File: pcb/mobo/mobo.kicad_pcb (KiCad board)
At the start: 2 copper layers, 51.6 x 89 mm, 73 parts, among them J1 ISP, J2 PEEL_MOTOR, J3 DRIVE_MOTOR, J4 SW1, J5 SPRING_FINGERS, J6 SW2, J8 USART1, U1 ATmega328PB-A, U2 ATmega328PB-M, U4 AP1117-50, U5 MC34063AD, U6 SP308xE, U7 DRV8837, U8 DRV8837, Y1 16MHz

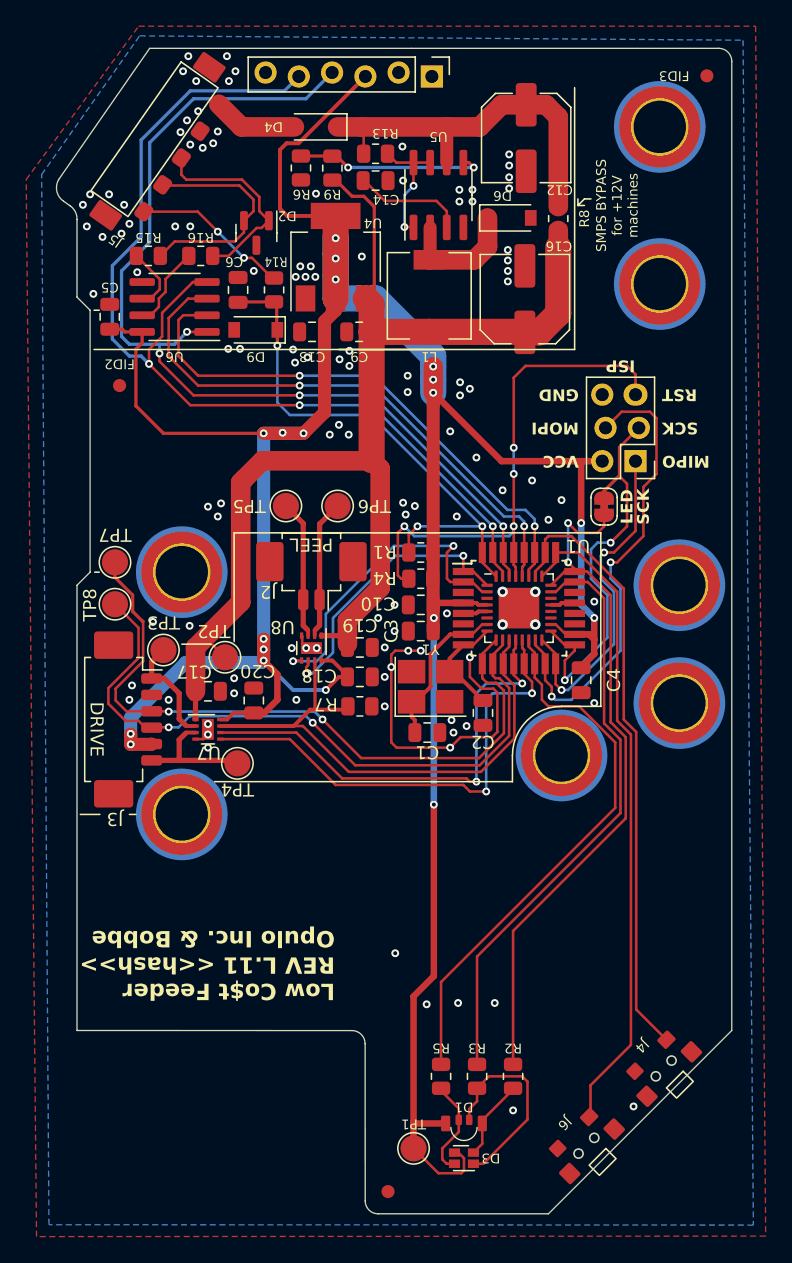
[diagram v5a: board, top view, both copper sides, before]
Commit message: Remove vias from pads, Remove paste layer from alt QFN footprint (#14)
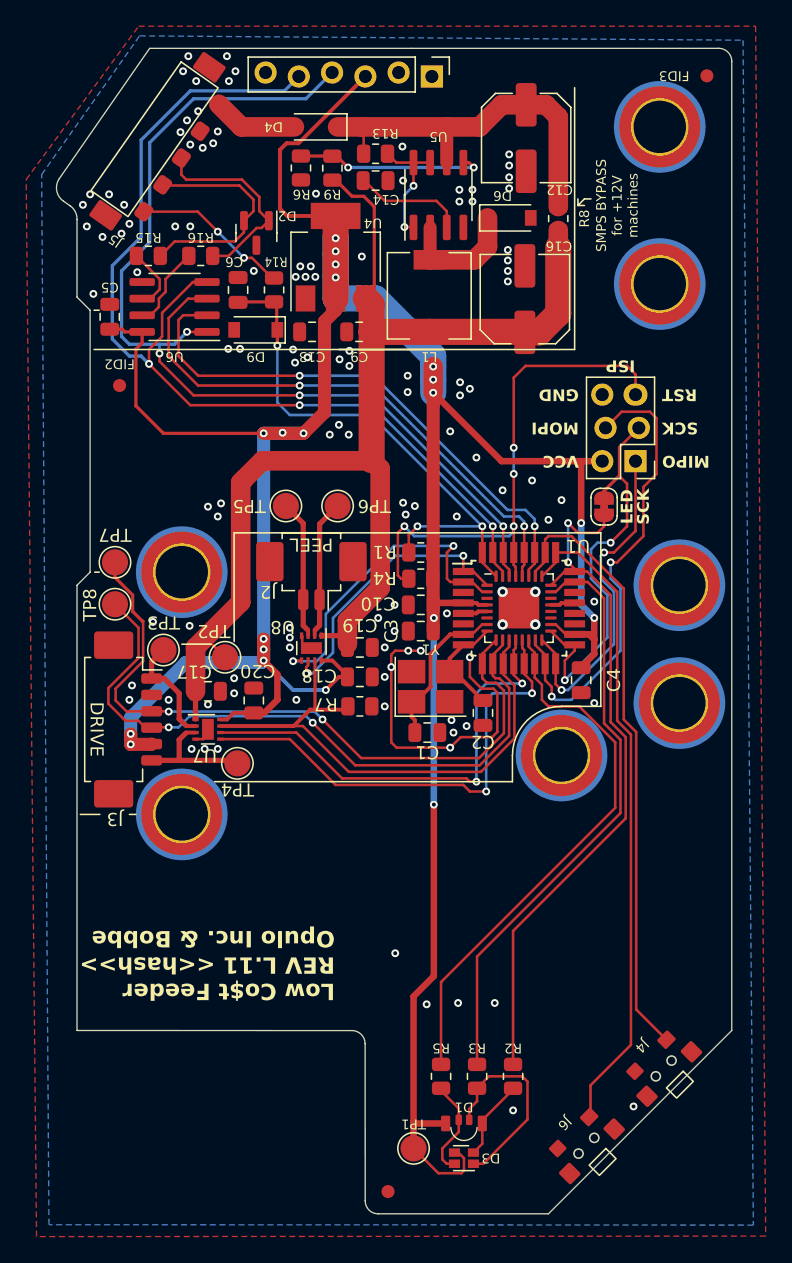
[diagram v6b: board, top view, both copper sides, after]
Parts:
- U2: footprint Package_DFN_QFN:QFN-32-1EP_5x5mm_P0.5mm_EP3.1x3.1mm -> feeder:QFN-32-1EP_5x5mm_P0.5mm_EP3.1x3.1mm_DNP
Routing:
- net GND: vias 117 -> 118
- net +5V: vias 19 -> 20

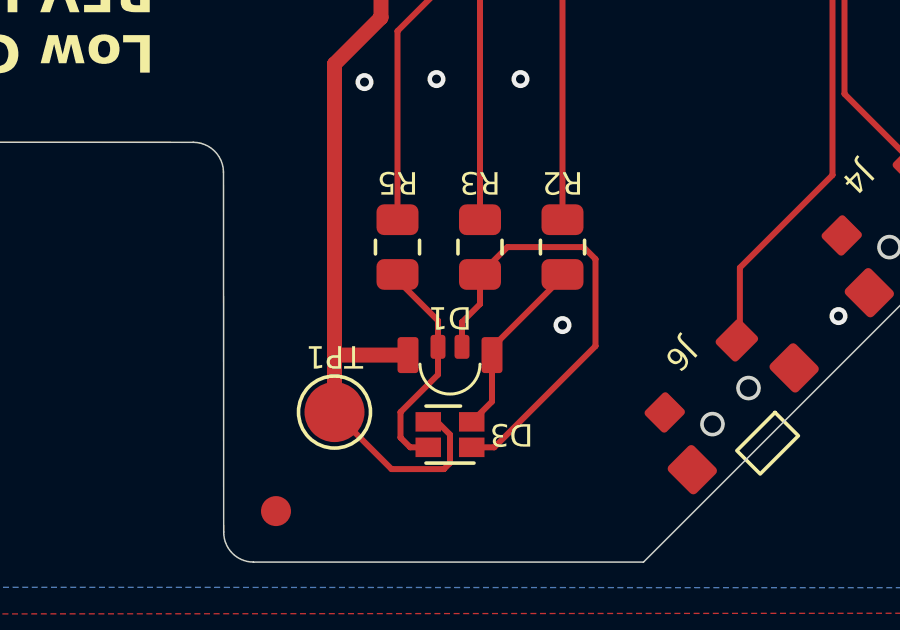
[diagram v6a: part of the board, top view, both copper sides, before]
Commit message: Mark LED_RGBA_ALT as DNP, Add MHS110FRGBCT symbol, footprint (#9)
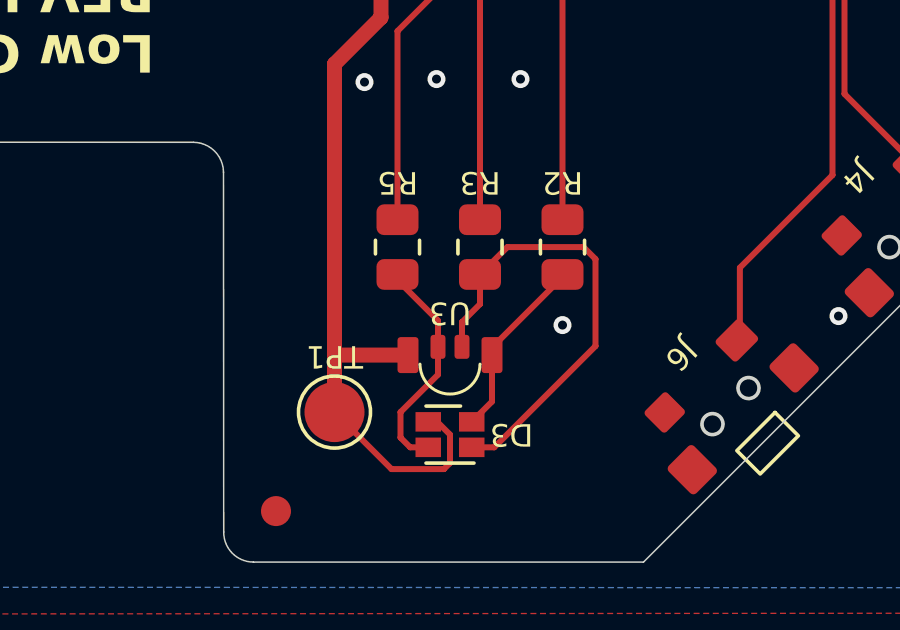
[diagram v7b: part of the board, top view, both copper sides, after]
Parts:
- U3: renamed from D1; value LED_RGBA -> LED_RGB; footprint index:MHS110FRGBCT -> feeder:MHS110FRGBCT
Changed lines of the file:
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@@
   (net 19 "DRIVE1")
   (net 20 "DE")
-  (net 21 "Net-(D1-GK)")
-  (net 22 "Net-(D1-BK)")
-  (net 23 "Net-(D1-A)")
+  (net 21 "Net-(D3-RK)")
+  (net 22 "Net-(D3-GK)")
+  (net 23 "Net-(D3-BK)")
   (net 24 "Net-(D6-K)")
   (net 25 "Net-(J5-Pin_5)")
@@
     )
   )
-  (footprint "index:MHS110FRGBCT" (layer "F.Cu")
+  (footprint "feeder:MHS110FRGBCT" (layer "F.Cu")
     (at 130.85 112.3)
     (property "Sheetfile" "mobo.kicad_sch")
     (property "Sheetname" "")
-    (property "ki_description" "RGB LED, red/green/blue/anode")
-    (property "ki_keywords" "LED RGB diode")
     (attr smd)
-    (fp_text reference "D1" (at 0 -1.65 180 unlocked) (layer "F.SilkS")
+    (fp_text reference "U3" (at 0 -1.8 180 unlocked) (layer "F.SilkS")
         (effects (font (size 0.75 0.75) (thickness 0.1)))
     )
-    (fp_text value "LED_RGBA" (at 0 1 unlocked) (layer "F.Fab")
+    (fp_text value "LED_RGB" (at 0 1 unlocked) (layer "F.Fab")
         (effects (font (size 1 1) (thickness 0.15)))
     )
@@
       (stroke (width 0.1) (type solid)) (layer "F.SilkS"))
     (pad "1" smd roundrect (at -1.4 -0.4) (size 0.7 1.2) (layers "F.Cu" "F.Paste" "F.Mask") (roundrect_rratio 0.1428571429)
-      (net 11 "+5V") (pinfunction "RK") (pintype "passive"))
+      (net 11 "+5V") (pinfunction "VCC") (pintype "unspecified"))
     (pad "2" smd roundrect (at -0.4 -0.675) (size 0.5 0.8) (layers "F.Cu" "F.Paste" "F.Mask") (roundrect_rratio 0.2)
-      (net 21 "Net-(D1-GK)") (pinfunction "GK") (pintype "passive"))
+      (net 23 "Net-(D3-BK)") (pinfunction "B") (pintype "unspecified"))
     (pad "3" smd roundrect (at 0.4 -0.675) (size 0.5 0.8) (layers "F.Cu" "F.Paste" "F.Mask") (roundrect_rratio 0.2)
-      (net 22 "Net-(D1-BK)") (pinfunction "BK") (pintype "passive"))
+      (net 22 "Net-(D3-GK)") (pinfunction "G") (pintype "unspecified"))
     (pad "4" smd roundrect (at 1.4 -0.4) (size 0.7 1.2) (layers "F.Cu" "F.Paste" "F.Mask") (roundrect_rratio 0.1428571429)
-      (net 23 "Net-(D1-A)") (pinfunction "A") (pintype "passive"))
+      (net 21 "Net-(D3-RK)") (pinfunction "R") (pintype "unspecified"))
   )
   (footprint "Package_SON:WSON-8-1EP_2x2mm_P0.5mm_EP0.9x1.6mm" (layer "F.Cu")
@@
       (net 38 "LED_B") (pintype "passive"))
     (pad "2" smd roundrect (at 0.9125 0 270) (size 1.025 1.4) (layers "F.Cu" "F.Paste" "F.Mask") (roundrect_rratio 0.243902439)
-      (net 21 "Net-(D1-GK)") (pintype "passive"))
+      (net 23 "Net-(D3-BK)") (pintype "passive"))
     (model "${KICAD6_3DMODEL_DIR}/Resistor_SMD.3dshapes/R_0805_2012Metric.wrl"
       (offset (xyz 0 0 0))
@@
       (net 37 "LED_G") (pintype "passive"))
     (pad "2" smd roundrect (at 0.9125 0 270) (size 1.025 1.4) (layers "F.Cu" "F.Paste" "F.Mask") (roundrect_rratio 0.243902439)
-      (net 22 "Net-(D1-BK)") (pintype "passive"))
+      (net 22 "Net-(D3-GK)") (pintype "passive"))
     (model "${KICAD6_3DMODEL_DIR}/Resistor_SMD.3dshapes/R_0805_2012Metric.wrl"
       (offset (xyz 0 0 0))
@@
       (net 41 "LED_R") (pintype "passive"))
     (pad "2" smd roundrect (at 0.9125 0 270) (size 1.025 1.4) (layers "F.Cu" "F.Paste" "F.Mask") (roundrect_rratio 0.243902439)
-      (net 23 "Net-(D1-A)") (pintype "passive"))
+      (net 21 "Net-(D3-RK)") (pintype "passive"))
     (model "${KICAD6_3DMODEL_DIR}/Resistor_SMD.3dshapes/R_0805_2012Metric.wrl"
       (offset (xyz 0 0 0))
@@
     (property "Sheetfile" "mobo.kicad_sch")
     (property "Sheetname" "")
+    (property "dnp" "")
     (property "ki_description" "RGB LED, red/green/blue/anode")
     (property "ki_keywords" "LED RGB diode")
@@
       (stroke (width 0.1) (type solid)) (layer "F.Fab"))
     (pad "1" smd rect (at -0.425 -0.725 270) (size 0.65 0.85) (layers "F.Cu" "F.Paste" "F.Mask")
-      (net 23 "Net-(D1-A)") (pinfunction "RK") (pintype "passive"))
+      (net 21 "Net-(D3-RK)") (pinfunction "RK") (pintype "passive"))
     (pad "2" smd rect (at 0.425 -0.725 270) (size 0.65 0.85) (layers "F.Cu" "F.Paste" "F.Mask")
-      (net 22 "Net-(D1-BK)") (pinfunction "GK") (pintype "passive"))
+      (net 22 "Net-(D3-GK)") (pinfunction "GK") (pintype "passive"))
     (pad "3" smd rect (at 0.425 0.725 270) (size 0.65 0.85) (layers "F.Cu" "F.Paste" "F.Mask")
-      (net 21 "Net-(D1-GK)") (pinfunction "BK") (pintype "passive"))
+      (net 23 "Net-(D3-BK)") (pinfunction "BK") (pintype "passive"))
     (pad "4" smd rect (at -0.425 0.725 270) (size 0.65 0.85) (layers "F.Cu" "F.Paste" "F.Mask")
       (net 11 "+5V") (pinfunction "A") (pintype "passive"))
@@
   (segment (start 135.05 65.55) (end 135.45 65.95) (width 0.2) (layer "B.Cu") (net 20))
   (segment (start 118.3 55.55) (end 123.9 55.55) (width 0.2) (layer "B.Cu") (net 20))
-  (segment (start 130.45 111.625) (end 130.45 112.550978) (width 0.2) (layer "F.Cu") (net 21))
-  (segment (start 130.45 112.550978) (end 129.2 113.800978) (width 0.2) (layer "F.Cu") (net 21))
-  (segment (start 129.2 113.800978) (end 129.2 114.65) (width 0.2) (layer "F.Cu") (net 21))
-  (segment (start 129.2 114.65) (end 129.525 114.975) (width 0.2) (layer "F.Cu") (net 21))
-  (segment (start 130.45 110.75) (end 129.1 109.4) (width 0.2) (layer "F.Cu") (net 21))
-  (segment (start 130.45 111.625) (end 130.45 110.75) (width 0.2) (layer "F.Cu") (net 21))
-  (segment (start 129.525 114.975) (end 130.125 114.975) (width 0.2) (layer "F.Cu") (net 21))
+  (segment (start 131.575 114.125) (end 132.25 113.45) (width 0.2) (layer "F.Cu") (net 21))
+  (segment (start 134.6 109.3) (end 132.25 111.65) (width 0.2) (layer "F.Cu") (net 21))
+  (segment (start 132.25 113.45) (end 132.25 111.9) (width 0.2) (layer "F.Cu") (net 21))
   (segment (start 131.85 109.2125) (end 131.85 110.2) (width 0.2) (layer "F.Cu") (net 22))
   (segment (start 135.7 111.6) (end 135.7 108.7) (width 0.2) (layer "F.Cu") (net 22))
@@
   (segment (start 132.325 114.975) (end 135.7 111.6) (width 0.2) (layer "F.Cu") (net 22))
   (segment (start 135.3 108.3) (end 132.7625 108.3) (width 0.2) (layer "F.Cu") (net 22))
-  (segment (start 131.575 114.125) (end 132.25 113.45) (width 0.2) (layer "F.Cu") (net 23))
-  (segment (start 134.6 109.3) (end 132.25 111.65) (width 0.2) (layer "F.Cu") (net 23))
-  (segment (start 132.25 113.45) (end 132.25 111.9) (width 0.2) (layer "F.Cu") (net 23))
+  (segment (start 130.45 111.625) (end 130.45 112.550978) (width 0.2) (layer "F.Cu") (net 23))
+  (segment (start 130.45 112.550978) (end 129.2 113.800978) (width 0.2) (layer "F.Cu") (net 23))
+  (segment (start 129.2 113.800978) (end 129.2 114.65) (width 0.2) (layer "F.Cu") (net 23))
+  (segment (start 129.2 114.65) (end 129.525 114.975) (width 0.2) (layer "F.Cu") (net 23))
+  (segment (start 130.45 110.75) (end 129.1 109.4) (width 0.2) (layer "F.Cu") (net 23))
+  (segment (start 130.45 111.625) (end 130.45 110.75) (width 0.2) (layer "F.Cu") (net 23))
+  (segment (start 129.525 114.975) (end 130.125 114.975) (width 0.2) (layer "F.Cu") (net 23))
   (segment (start 132.65 44.95) (end 131.65 45.95) (width 1.5) (layer "F.Cu") (net 24))
   (segment (start 128.265 45.885) (end 128.2 45.95) (width 1.5) (layer "F.Cu") (net 24))

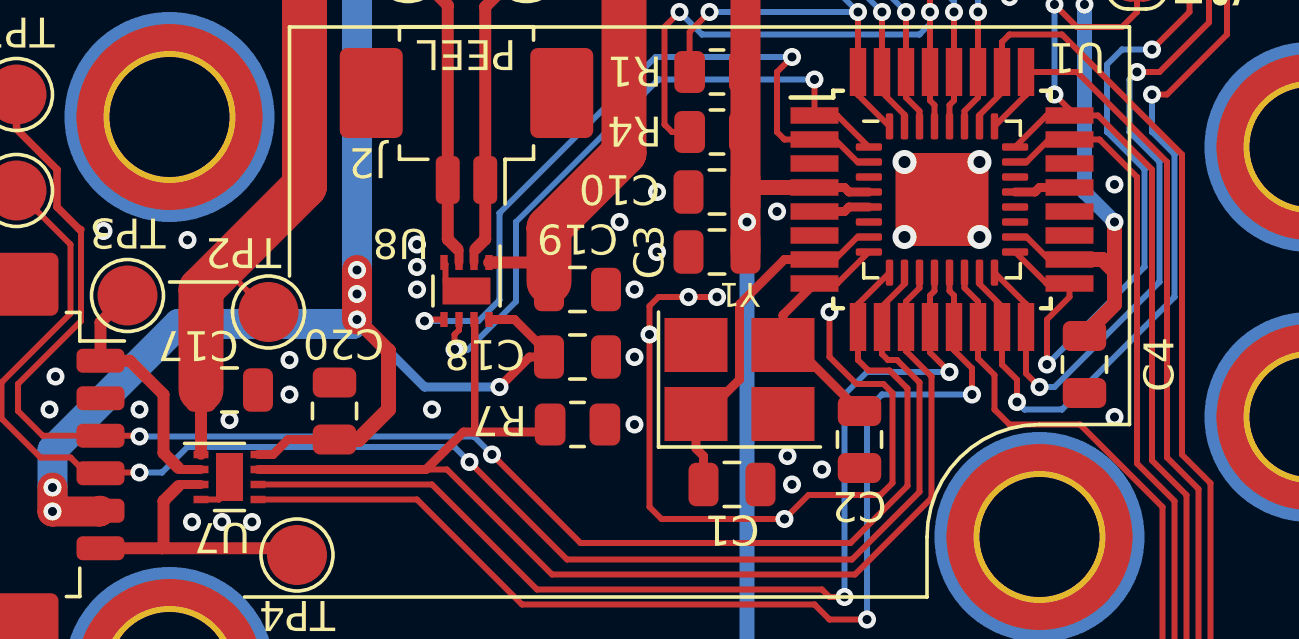
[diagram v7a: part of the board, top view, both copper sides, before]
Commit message: Improve driver power routing by adding filled zones
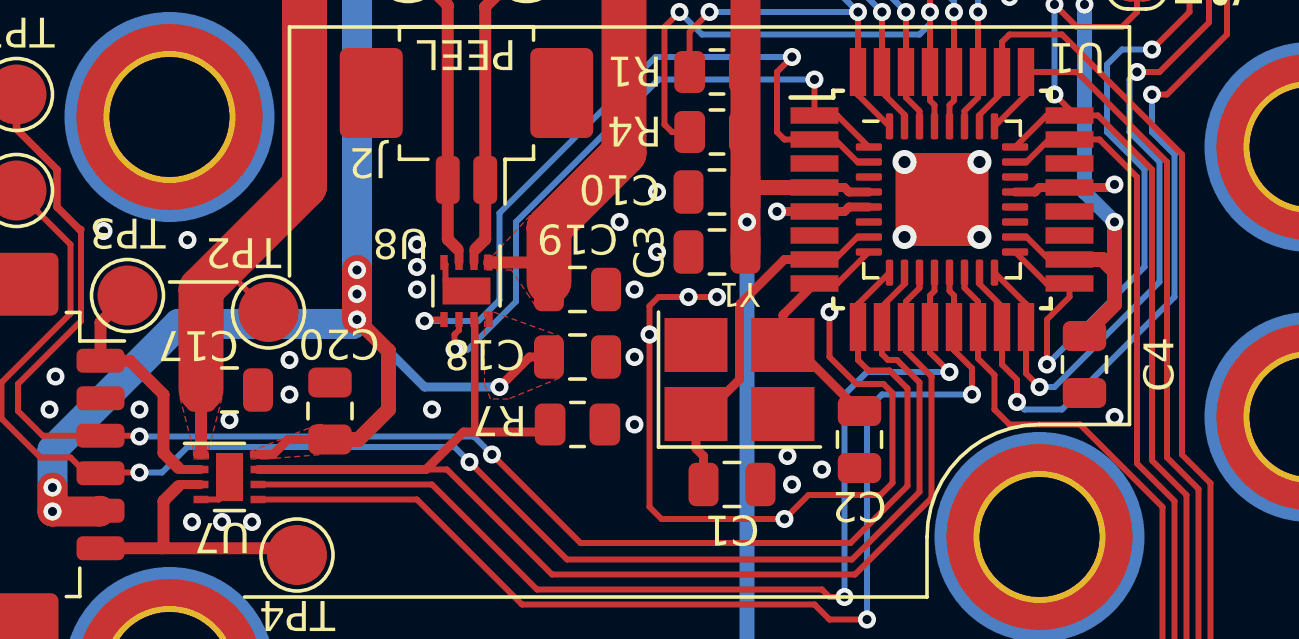
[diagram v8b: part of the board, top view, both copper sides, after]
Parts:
- moved C20 0.15 mm to (114.7, 79.6)
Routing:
- net GND: track 30.4 -> 33.2 mm
- net +5V: track 242.0 -> 239.5 mm
- added copper zone on F.Cu, net (none)
- added copper zone on F.Cu, net +10V
- added copper zone on F.Cu, net +5V
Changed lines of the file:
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@@
   )
   (footprint "Capacitor_SMD:C_0805_2012Metric" (layer "F.Cu")
-    (at 114.8 79.6 -90)
+    (at 114.65 79.6 -90)
     (descr "Capacitor SMD 0805 (2012 Metric), square (rectangular) end terminal, IPC_7351 nominal, (Body size source: IPC-SM-782 page 76, https://www.pcb-3d.com/wordpress/wp-content/uploads/ipc-sm-782a_amendment_1_and_2.pdf, https://docs.google.com/spreadsheets/d/1BsfQQcO9C6DZCsRaXUlFlo91Tg2WpOkGARC1WS5S8t0/edit?usp=sharing), generated with kicad-footprint-generator")
     (tags "capacitor")
@@
   )
   (segment (start 125.3 82.8) (end 125.3 76.1) (width 0.2) (layer "F.Cu") (net 1))
+  (segment (start 140.7 72.15) (end 140.8 72.05) (width 0.3) (layer "F.Cu") (net 1))
   (segment (start 129.8 83.2) (end 125.7 83.2) (width 0.2) (layer "F.Cu") (net 1))
   (segment (start 132.6125 72.8) (end 131.95 72.8) (width 0.3) (layer "F.Cu") (net 1))
@@
   (segment (start 131.95 72.8) (end 131.8 72.95) (width 0.3) (layer "F.Cu") (net 1))
   (segment (start 133.4 79) (end 133.4 82) (width 0.2) (layer "F.Cu") (net 1))
+  (segment (start 130.8 72.95) (end 129.55 72.95) (width 0.3) (layer "F.Cu") (net 1))
   (segment (start 133.4 82) (end 133 82.4) (width 0.2) (layer "F.Cu") (net 1))
   (segment (start 125.3 76.1) (end 125.6 75.8) (width 0.2) (layer "F.Cu") (net 1))
+  (segment (start 139.3 72.15) (end 140.7 72.15) (width 0.3) (layer "F.Cu") (net 1))
   (segment (start 138.3 72.15) (end 139.3 72.15) (width 0.3) (layer "F.Cu") (net 1))
   (segment (start 131.8 72.95) (end 130.8 72.95) (width 0.3) (layer "F.Cu") (net 1))
@@
   (segment (start 140.8 74.95) (end 140.4 74.55) (width 0.5) (layer "F.Cu") (net 11))
   (segment (start 130.85 114.55) (end 130.85 115.499022) (width 0.2) (layer "F.Cu") (net 11))
-  (segment (start 119.95 76.55) (end 120.8 76.55) (width 0.3) (layer "F.Cu") (net 11))
   (segment (start 130.425 114.125) (end 130.85 114.55) (width 0.2) (layer "F.Cu") (net 11))
   (segment (start 112.25 81.05) (end 112.75 81.05) (width 0.3) (layer "F.Cu") (net 11))
@@
   (segment (start 132.6125 72.3) (end 131.95 72.3) (width 0.3) (layer "F.Cu") (net 11))
   (segment (start 106.275 51.455) (end 104.955 51.455) (width 0.25) (layer "F.Cu") (net 11))
-  (segment (start 121.95 77.7) (end 120.8 76.55) (width 0.3) (layer "F.Cu") (net 11))
   (segment (start 120.2 51.45) (end 120.2 57.6) (width 1) (layer "F.Cu") (net 11))
   (segment (start 116.6 79.55) (end 116.6 77.6) (width 0.5) (layer "F.Cu") (net 11))
@@
       )
     )
+  )
+  (zone (net 0) (net_name "") (layer "F.Cu") (hatch edge 0.5)
+    (priority 4)
+    (connect_pads yes (clearance 0.2))
+    (min_thickness 0.1) (filled_areas_thickness no)
+    (fill yes (thermal_gap 0.5) (thermal_bridge_width 0.5))
+    (polygon
+      (pts
+        (xy 112 81.2)
+        (xy 112.5 81.2)
+        (xy 114.4 81.05)
+        (xy 114.4 80.05)
+        (xy 114.25 80.05)
+        (xy 112 80.95)
+      )
+    )
+  )
+  (zone (net 15) (net_name "+10V") (layer "F.Cu") (hatch edge 0.5)
+    (priority 3)
+    (connect_pads yes (clearance 0.2))
+    (min_thickness 0.1) (filled_areas_thickness no)
+    (fill yes (thermal_gap 0.5) (thermal_bridge_width 0.5))
+    (polygon
+      (pts
+        (xy 110.6 80.9)
+        (xy 111.05 79.15)
+        (xy 109.65 79.15)
+        (xy 110.1 80.9)
+        (xy 110.1 81.2)
+        (xy 110.6 81.2)
+      )
+    )
+  )
+  (zone (net 11) (net_name "+5V") (layer "F.Cu") (hatch edge 0.5)
+    (priority 2)
+    (connect_pads yes (clearance 0.2))
+    (min_thickness 0.1) (filled_areas_thickness no)
+    (fill yes (thermal_gap 0.5) (thermal_bridge_width 0.5))
+    (polygon
+      (pts
+        (xy 119.8 76.3)
+        (xy 120.1 76.3)
+        (xy 122.3 77.1)
+        (xy 122.3 78.5)
+        (xy 120.6 79.2)
+        (xy 120 79.2)
+        (xy 119.8 78.7)
+        (xy 119.8 77.4)
+        (xy 119.8 76.8)
+      )
+    )
+  )
+  (zone (net 15) (net_name "+10V") (layer "F.Cu") (hatch edge 0.5)
+    (priority 1)
+    (connect_pads yes (clearance 0.2))
+    (min_thickness 0.1) (filled_areas_thickness no)
+    (fill yes (thermal_gap 0.5) (thermal_bridge_width 0.5))
+    (polygon
+      (pts
+        (xy 119.8 74.4)
+        (xy 120.1 74.4)
+        (xy 121.4 73)
+        (xy 122.3 74)
+        (xy 122.3 76.1)
+        (xy 121.5 76.1)
+        (xy 121.3 75.8)
+        (xy 120.7 74.9)
+        (xy 119.8 74.9)
+      )
+    )
